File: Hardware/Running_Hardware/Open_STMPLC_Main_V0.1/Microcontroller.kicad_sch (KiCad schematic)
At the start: 46 parts, among them J1 Conn_02x08_Odd_Even, J2 USB C, SW1 Switch, U1 STM32F407ZGTx, U3 TPS3430WDRC, U4 CH340C, Y1 48MHz, Y2 32.768kHz

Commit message: Main PCB changes
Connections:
- net +3V3: now also J1.2 (Pin_2)
- no-connect marks 11 -> 12
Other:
- note added: "IO Expander"
- moved on the sheet: J1

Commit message: Main PCB component placement
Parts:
- removed U1: STM32F407ZGTx, Package_QFP:LQFP-144_20x20mm_P0.5mm, symbol MCU_ST_STM32F4:STM32F407ZGTx
- added C59, C60, C63: 100nF, Capacitor_SMD:C_0603_1608Metric_Pad1.08x0.95mm_HandSolder, symbol Device:C_Small
- added C61, C62: 2.2uF, Capacitor_SMD:C_0603_1608Metric_Pad1.08x0.95mm_HandSolder, symbol Device:C_Small
- added C64: 1uF, Capacitor_SMD:C_0603_1608Metric_Pad1.08x0.95mm_HandSolder, symbol Device:C_Small
- added U1: STM32F407IGTx, Package_QFP:LQFP-176_24x24mm_P0.5mm, symbol MCU_ST_STM32F4:STM32F407IGTx
- SW1: footprint Button_Switch_SMD:SW_SPST_PTS810 -> Button_Switch_THT:SW_PUSH_6mm_H5mm
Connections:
- net GND: now also C59.2, C60.2, C61.2, C62.2, C63.2, C64.2, U1.102 (VSS), U1.113 (VSS), U1.126 (VSS), U1.135 (VSS), U1.14 (VSS), U1.148 (VSS), U1.158 (VSS), U1.22 (VSS), U1.37 (VSSA), U1.61 (VSS), U1.71 (VSS), U1.90 (VSS)
- net ~{WDO}: now also U1.31 (NRST)
- net at C3.1, Y1.1: now also U1.30 (PH1)
- net 3V3_MCU: now reaches C10.1, C11.1, C12.1, C13.1, C14.1, C16.1, C18.1, C21.1, C23.1, C24.1, C26.1, C27.1, C8.1, C9.1, R1.1, R3.2
- net 3V3_MCU: now also C59.1, C60.1, C63.1, C64.1, U1.103 (VDD), U1.114 (VDD), U1.127 (VDD), U1.136 (VDD), U1.149 (VDD), U1.15 (VDD), U1.159 (VDD), U1.172 (VDD), U1.23 (VDD), U1.36 (VDD), U1.38 (VREF+), U1.39 (VDDA), U1.49 (VDD), U1.62 (VDD), U1.72 (VDD), U1.82 (VDD), U1.91 (VDD)
- net at R2.2: now also U1.166 (BOOT0)
- net at C2.1, Y1.3: now also U1.29 (PH0)
- net at D1.1 (K): now also U1.6 (VBAT)
- net at C19.1, Y2.2: now also U1.9 (PC14)
- net at C20.1, Y2.1: now also U1.10 (PC15)
- new net: C61.1, U1.125 (VCAP_2)
- new net: C62.1, U1.81 (VCAP_1)
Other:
- moved on the sheet: BT1, C1, C10, C11, C12, C13, C14, C16, C18, C19, C2, C20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

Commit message: Schematic updates
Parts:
- removed R3: 0R, Resistor_SMD:R_0603_1608Metric_Pad0.98x0.95mm_HandSolder, symbol Device:R_Small
- added C70: 100nF, Capacitor_SMD:C_0603_1608Metric_Pad1.08x0.95mm_HandSolder, symbol Device:C_Small
- added FB2: BLM21PG121SN1D, Inductor_SMD:L_0805_2012Metric_Pad1.05x1.20mm_HandSolder, symbol Device:FerriteBead_Small
- added J12: USB C, Connector_USB:USB_C_Receptacle_GCT_USB4105-xx-A_16P_TopMnt_Horizontal, symbol Connector:USB_C_Receptacle_USB2.0
- added J3: Conn_01x04, Connector_JST:JST_XH_B4B-XH-A_1x04_P2.50mm_Vertical, symbol Connector_Generic:Conn_01x04
- added R17, R30: 10K, Resistor_SMD:R_0603_1608Metric_Pad0.98x0.95mm_HandSolder, symbol Device:R_Small
- added R32: 0R, Resistor_SMD:R_0603_1608Metric_Pad0.98x0.95mm_HandSolder, symbol Device:R_Small
- added R33, R37: 5.1K, Resistor_SMD:R_0603_1608Metric_Pad0.98x0.95mm_HandSolder, symbol jlcpcb-basic-resistor-0805:4.7k
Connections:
- net +3V3: now also C70.2, FB2.2, J3.1 (Pin_1), R17.2, R30.2
- net +5V: now also R32.2
- net 3V3_MCU: now also FB2.1
- net GND: now also C70.1, J12.A1 (GND), J12.A12 (GND), J12.B1 (GND), J12.B12 (GND), J12.S1 (SHIELD), J3.2 (Pin_2), R33.1, R37.1
- net STM_DN: now also J12.A7 (D-), J12.B7 (D-); no longer J2.A7 (D-), J2.B7 (D-), U4.6 (UD-)
- net STM_DP: now also J12.A6 (D+), J12.B6 (D+); no longer J2.A6 (D+), J2.B6 (D+), U4.5 (UD+)
- new net: J12.A5 (CC1), R37.2
- new net: J12.A4 (VBUS), J12.A9 (VBUS), J12.B4 (VBUS), J12.B9 (VBUS), R32.1
- new net: J12.B5 (CC2), R33.2
- new net DEBUG_DN: J2.A7 (D-), J2.B7 (D-), U4.6 (UD-)
- new net DEBUG_DP: J2.A6 (D+), J2.B6 (D+), U4.5 (UD+)
- new net DISP_SCL: J3.3 (Pin_3), R17.1
- new net DISP_SDA: J3.4 (Pin_4), R30.1
- no-connect marks 12 -> 14
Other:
- note added: "DISPLAY"
- moved on the sheet: C28, C29, C30, C31, J1, J2, R10, R11, R12, R13, R4, R5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

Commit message: Component placement main pcb
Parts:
- added R3: 0R, Resistor_SMD:R_0603_1608Metric_Pad0.98x0.95mm_HandSolder, symbol Device:R_Small
- J3: footprint Connector_JST:JST_XH_B4B-XH-A_1x04_P2.50mm_Vertical -> Connector_PinHeader_2.54mm:PinHeader_1x04_P2.54mm_Horizontal
- SW1: value Switch -> Switch_6x6; footprint Button_Switch_THT:SW_PUSH_6mm_H5mm -> Button_Switch_SMD:SW_Push_1P1T_NO_E-Switch_TL3301NxxxxxG
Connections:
- net +3V3: now also J3.4 (Pin_4); no longer J3.1 (Pin_1)
- net DISP_SCL: now also J3.2 (Pin_2); no longer J3.3 (Pin_3)
- net DISP_SDA: now also J3.1 (Pin_1); no longer J3.4 (Pin_4)
- net ETH_CRSDV: now also U1.53 (PA7)
- net ETH_MDC: now also U1.33 (PC1)
- net ETH_MDIO: now also U1.42 (PA2)
- net ETH_RXD0: now also U1.54 (PC4)
- net ETH_RXD1: now also U1.55 (PC5)
- net ETH_TXD0: now also U1.156 (PG13)
- net ETH_TXD1: now also U1.157 (PG14)
- net ETH_TXEN: now also U1.154 (PG11)
- net GND: now also J3.3 (Pin_3); no longer J3.2 (Pin_2)
- net SD_CLK: now also U1.141 (PC12)
- net ~{WDO}: now also R3.1; no longer C1.1, R1.2, SW1.2, U1.31 (NRST)
- net SD_DAT0: now reaches U1.117 (PC8)
- net SD_DAT1: now reaches U1.118 (PC9)
- net SD_DAT2: now reaches U1.139 (PC10)
- net SD_DAT3: now reaches U1.140 (PC11)
- net SD_CMD: now reaches U1.144 (PD2)
- net ETH_REFCLKO: now reaches U1.41 (PA1)
- new net ~{STM_RST}: C1.1, R1.2, R3.2, SW1.2, U1.31 (NRST)
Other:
- moved on the sheet: C19, C20, Y2

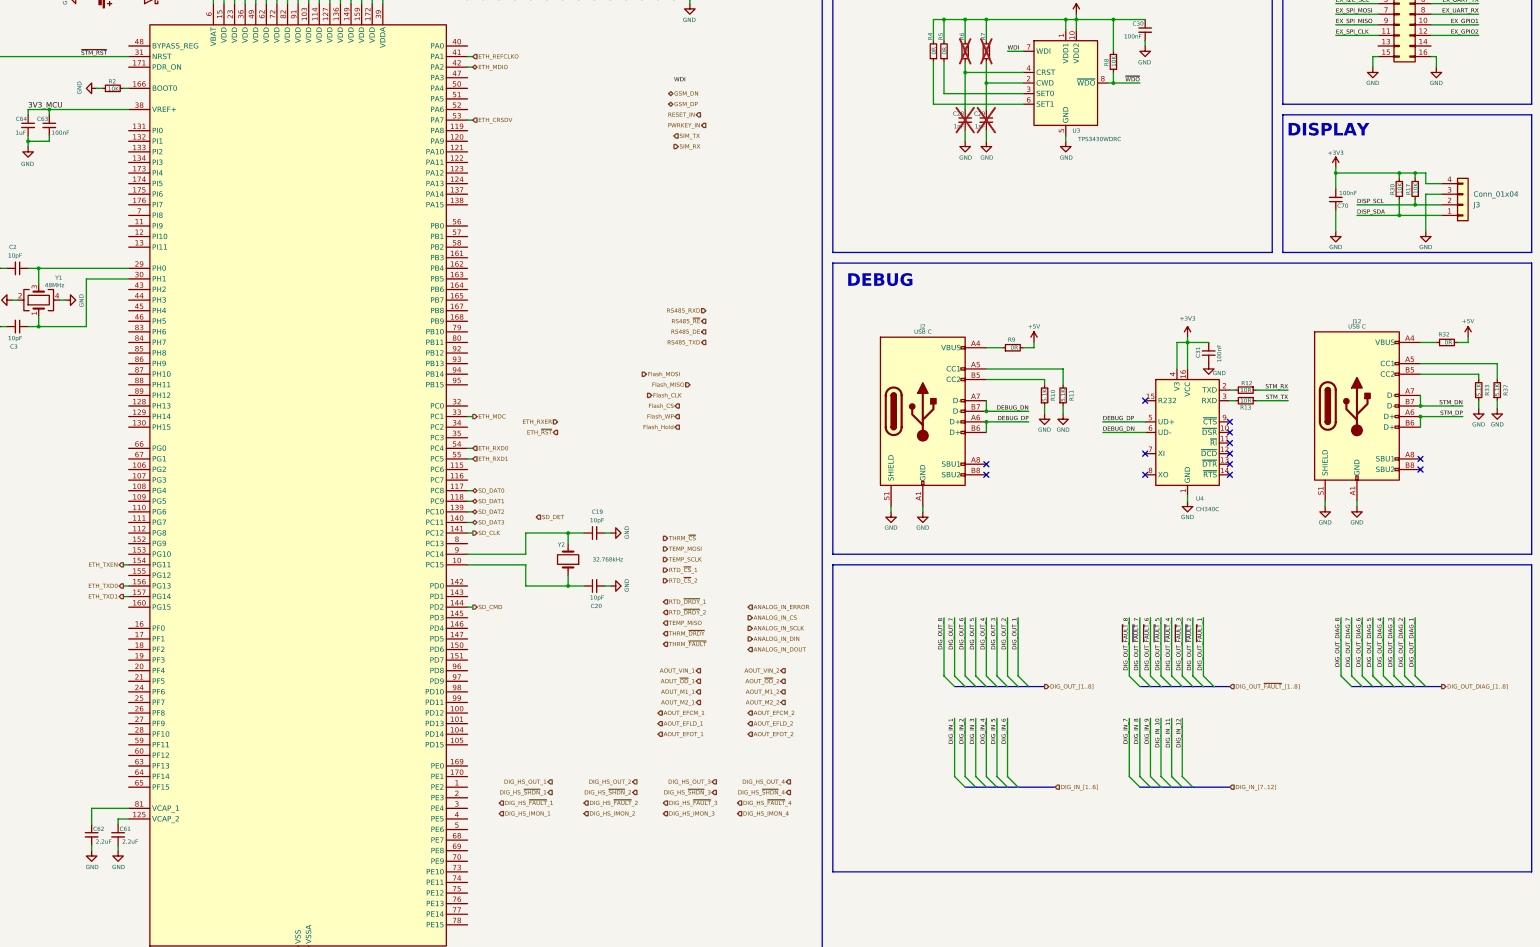
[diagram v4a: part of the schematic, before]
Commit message: Layer stack up main PCB and pin mapping
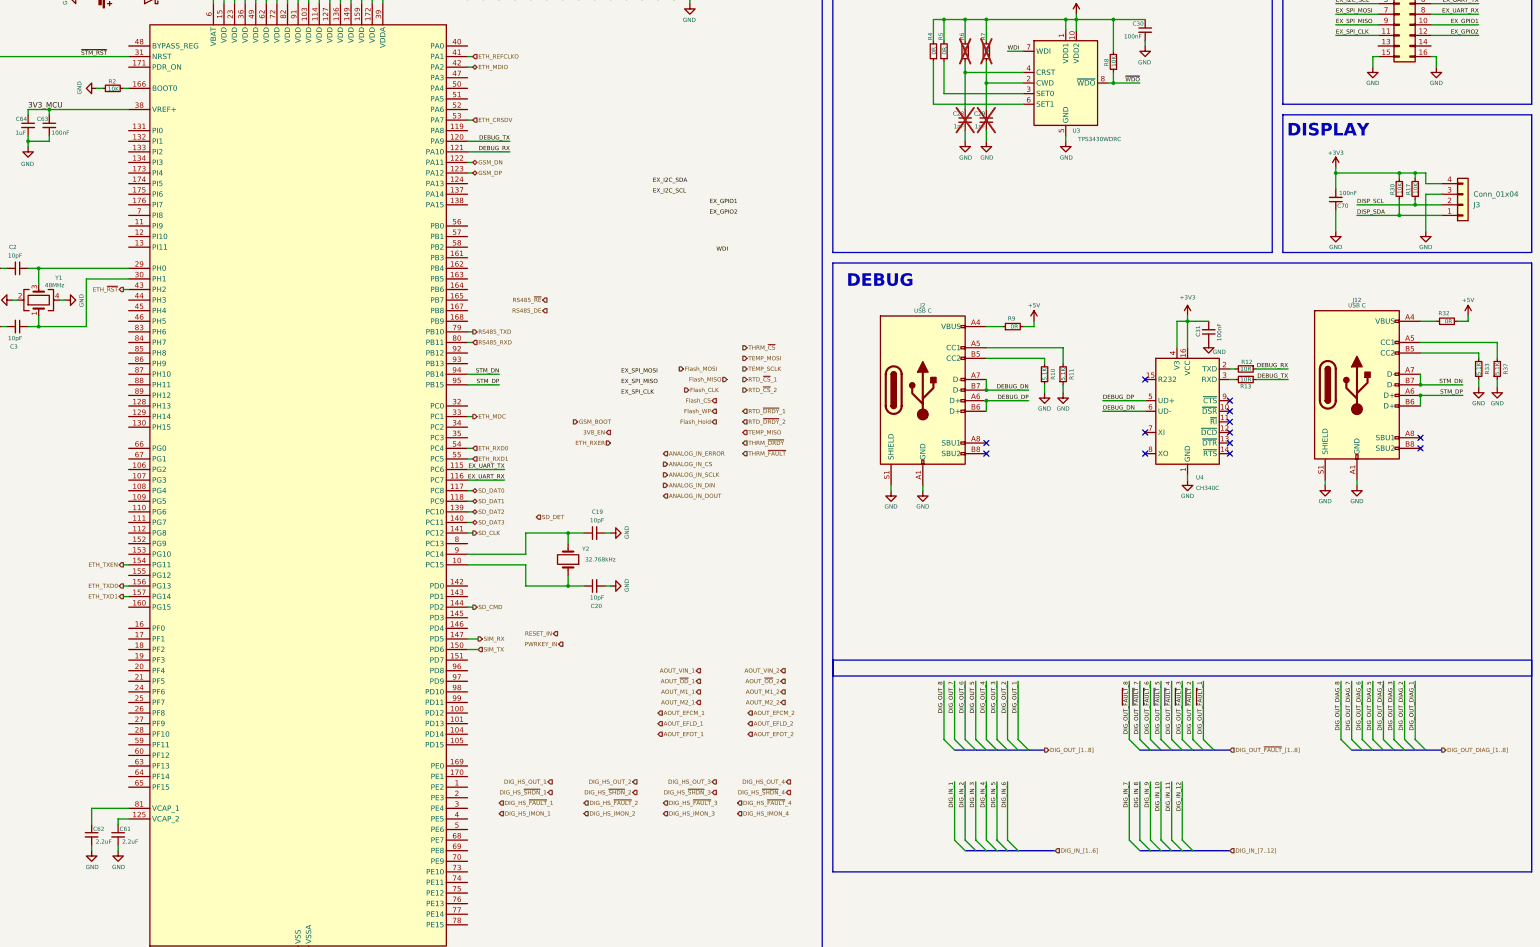
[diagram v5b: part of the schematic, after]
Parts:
- BT1: footprint Battery:BatteryHolder_MYOUNG_BS-07-A1BJ001_CR2032 -> Battery:BatteryHolder_Multicomp_BC-2001_1x2032
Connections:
- net STM_RX is gone; now on net DEBUG_RX: R12.1
- net STM_TX is gone; now on net DEBUG_TX: R13.1
- net ETH_~{RST}: now also U1.43 (PH2)
- net EX_UART_RX: now also U1.116 (PC7)
- net EX_UART_TX: now also U1.115 (PC6)
- net GSM_DN: now also U1.122 (PA11)
- net GSM_DP: now also U1.123 (PA12)
- net RS485_RXD: now also U1.80 (PB11)
- net RS485_TXD: now also U1.79 (PB10)
- net SIM_RX: now also U1.147 (PD5)
- net SIM_TX: now also U1.150 (PD6)
- net STM_DN: now also U1.94 (PB14)
- net STM_DP: now also U1.95 (PB15)
- net DEBUG_TX: now reaches U1.120 (PA9)
- net DEBUG_RX: now reaches U1.121 (PA10)
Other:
- moved on the sheet: C31, J12, J2, R10, R11, R12, R13, R32, R33, R37, R9, U4

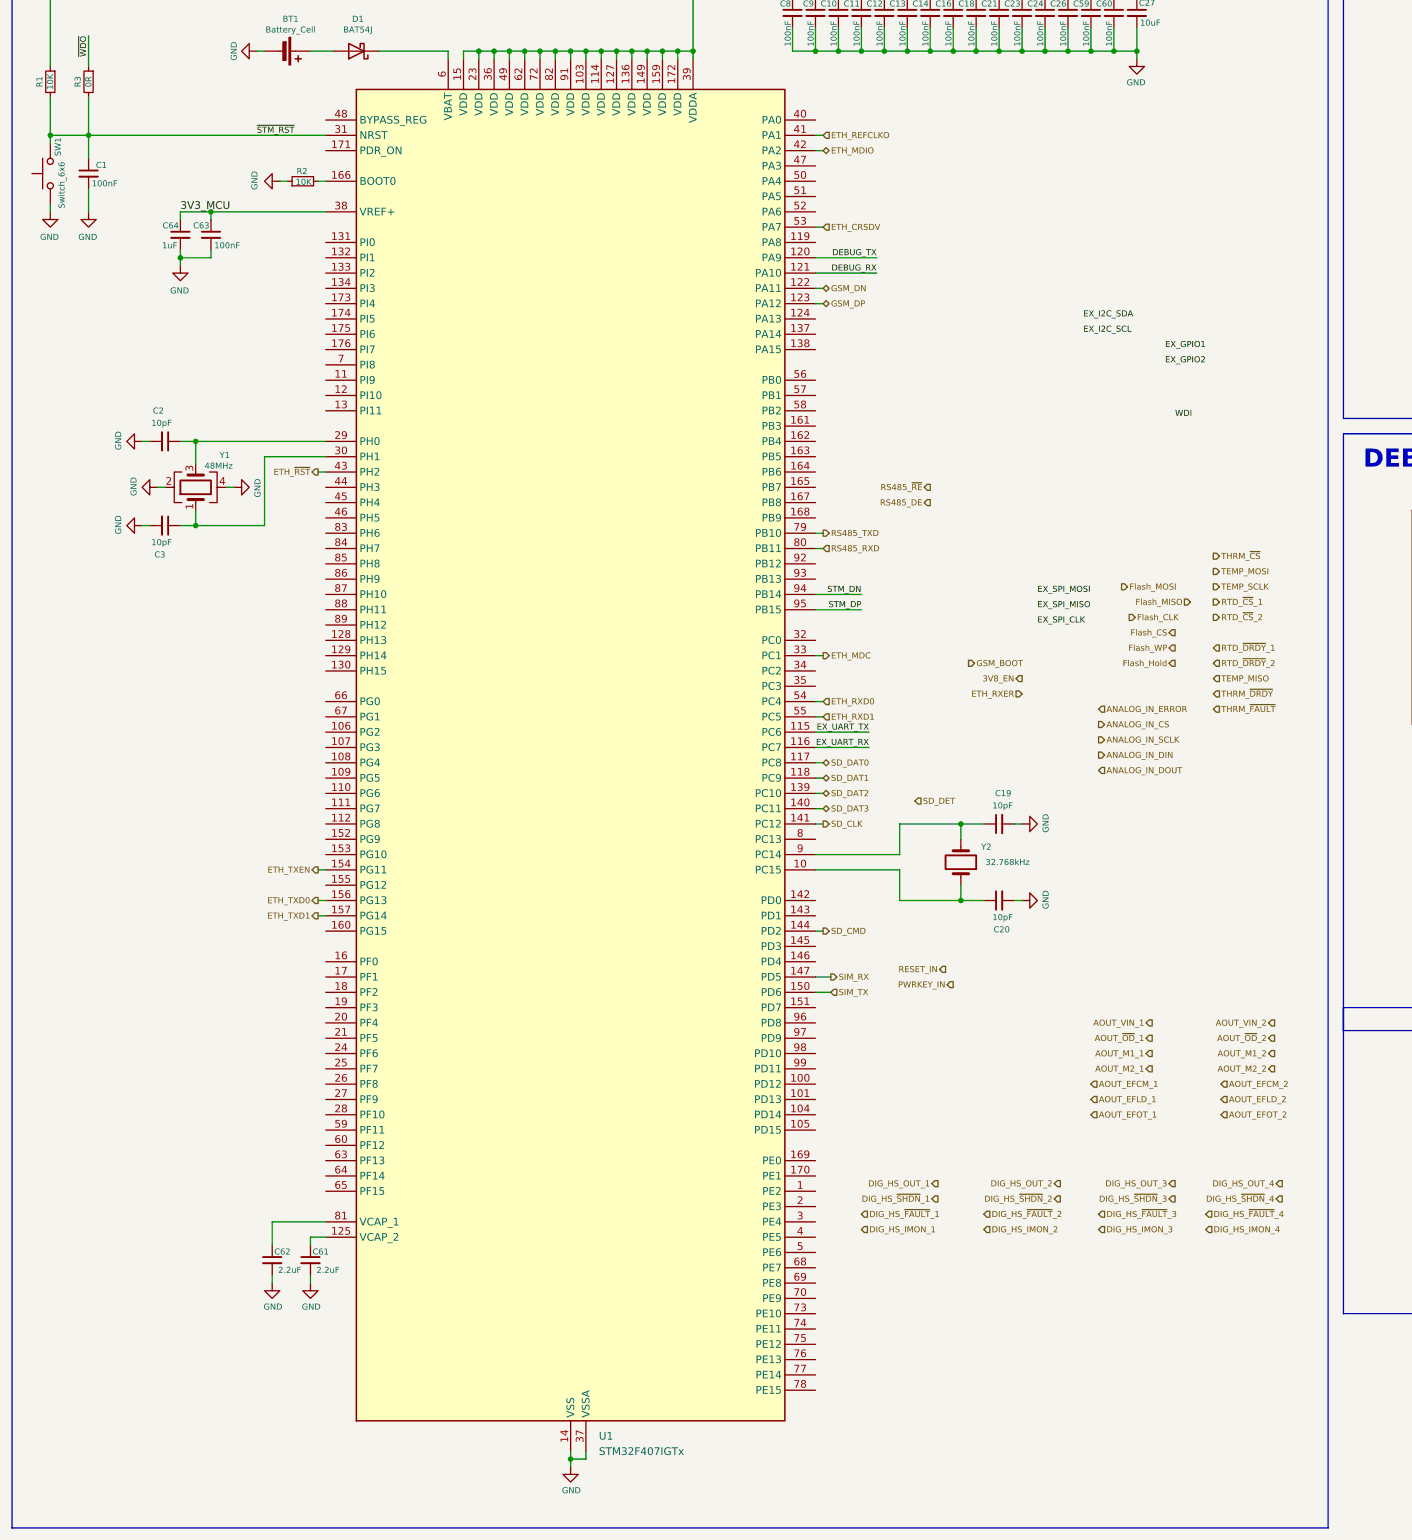
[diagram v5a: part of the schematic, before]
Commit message: MCU pin mapping
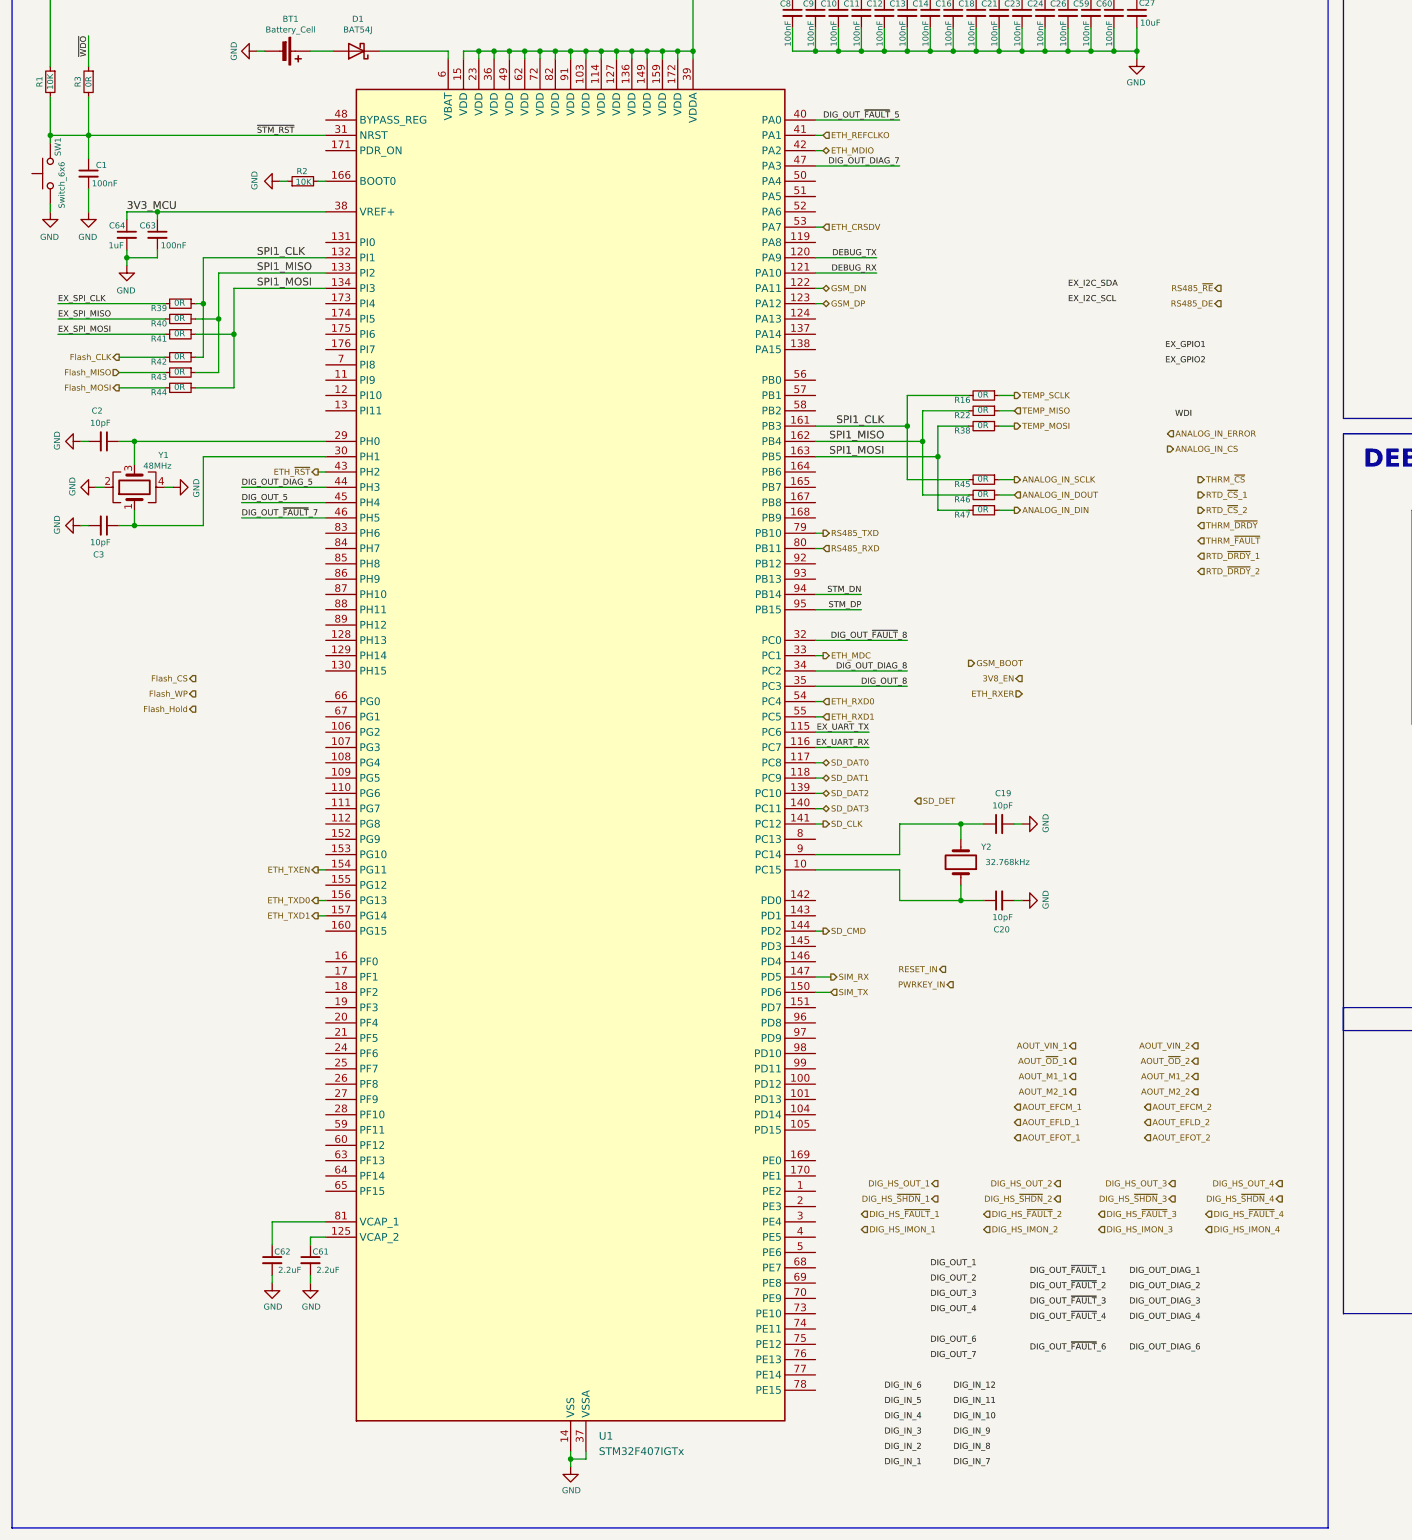
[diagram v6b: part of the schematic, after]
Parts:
- added R16, R22, R38, R39, R40, R41, R42, R43, R44, R45, R46, R47: 0R, Resistor_SMD:R_0603_1608Metric_Pad0.98x0.95mm_HandSolder, symbol Device:R_Small
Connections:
- net ANALOG_IN_DIN: now also R47.1
- net ANALOG_IN_DOUT: now also R46.1
- net ANALOG_IN_SCLK: now also R45.1
- net DIG_OUT_5: now also U1.45 (PH4)
- net DIG_OUT_8: now also U1.35 (PC3)
- net DIG_OUT_DIAG_5: now also U1.44 (PH3)
- net DIG_OUT_DIAG_7: now also U1.47 (PA3)
- net DIG_OUT_DIAG_8: now also U1.34 (PC2)
- net DIG_OUT_~{FAULT}_5: now also U1.40 (PA0)
- net DIG_OUT_~{FAULT}_7: now also U1.46 (PH5)
- net DIG_OUT_~{FAULT}_8: now also U1.32 (PC0)
- net EX_SPI_CLK: now also R39.2
- net EX_SPI_MISO: now also R40.2
- net EX_SPI_MOSI: now also R41.2
- net Flash_CLK: now also R42.2
- net Flash_MISO: now also R43.2
- net Flash_MOSI: now also R44.2
- net TEMP_MISO: now also R22.1
- net TEMP_MOSI: now also R38.1
- net TEMP_SCLK: now also R16.1
- net SPI1_CLK: now reaches U1.132 (PI1)
- net SPI1_CLK: now also U1.161 (PB3), R16.2, R39.1, R42.1, R45.2
- net SPI1_MISO: now reaches U1.133 (PI2)
- net SPI1_MISO: now also U1.162 (PB4), R22.2, R40.1, R43.1, R46.2
- net SPI1_MOSI: now reaches U1.134 (PI3)
- net SPI1_MOSI: now also U1.163 (PB5), R38.2, R41.1, R44.1, R47.2
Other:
- moved on the sheet: C2, C3, C63, C64, Y1
